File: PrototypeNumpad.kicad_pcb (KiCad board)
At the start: 2 copper layers, 99 x 99 mm, 86 parts, among them J0 Conn_01x06, J1 USB_B_Micro, SW0 SW_Push, U1 ATmega32U4-AU, U2 USBLC6-2SC6, Y1 Crystal_GND24

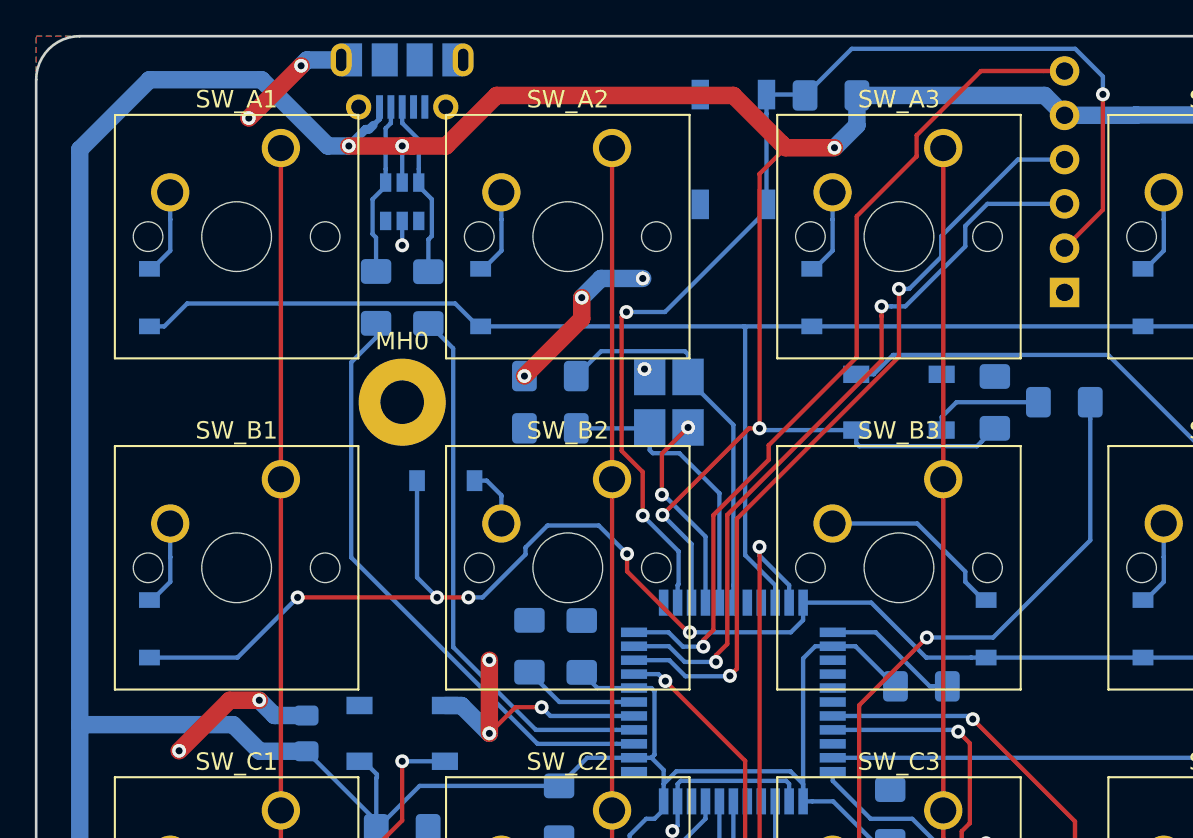
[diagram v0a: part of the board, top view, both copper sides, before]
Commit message: Add Header References
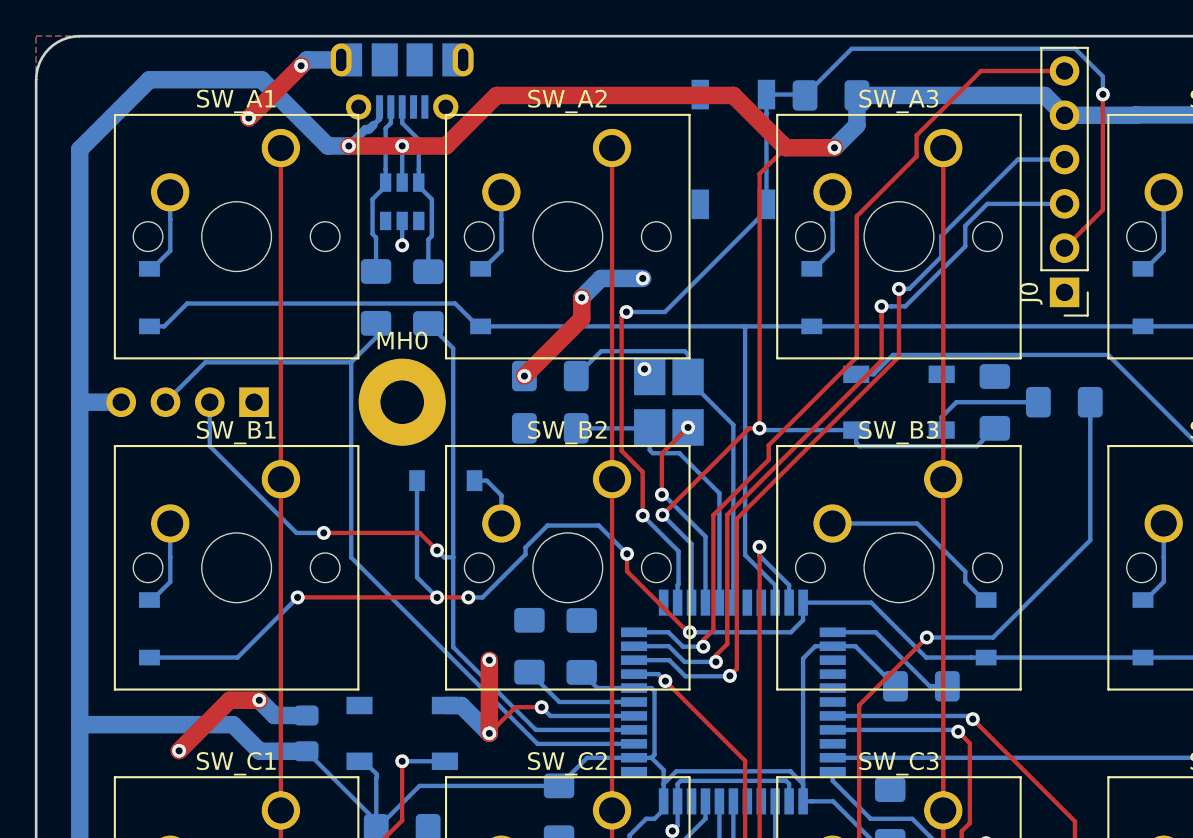
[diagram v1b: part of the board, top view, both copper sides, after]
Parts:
- added J1A1: Conn_01x04, Connector_PinHeader_2.54mm:PinHeader_1x04_P2.54mm_Vertical, B.Cu at (61.0, 49.5)
- J0: moved to F.Cu
- turned J0 to 180 degrees
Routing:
- net D+: track 31.5 -> 50.6 mm, vias 0 -> 2
- net D-: track 34.7 -> 46.3 mm
- net VCC: track 449.1 -> 451.5 mm
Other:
- board text added: "D+"
- board text added: "D-"
- board text added: "GND"
- board text added: "MISO"
- board text added: "MOSI"
- board text added: "RST"
- board text added: "SCK"
- board text added: "VCC"

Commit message: Re-position capacitor C9
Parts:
- moved C9 34.2 mm to (92.5, 49.5)
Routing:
- net GND: track 78.0 -> 69.2 mm, vias 20 -> 19
- net VCC: track 451.5 -> 449.5 mm
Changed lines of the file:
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@@
     (thickness 1.6)
     (drawings 18)
-    (tracks 657)
+    (tracks 649)
     (zones 0)
     (modules 87)
@@
   )
   (setup
-    (last_trace_width 0.25)
+    (last_trace_width 1)
     (user_trace_width 0.3)
     (user_trace_width 0.5)
@@
   )
   (module Capacitor_SMD:C_0805_2012Metric_Pad1.15x1.40mm_HandSolder (layer B.Cu)
-    (at 64 68.5 90)
+    (at 92.5 49.525 90)
     (descr "Capacitor SMD 0805 (2012 Metric), square (rectangular) end terminal, IPC_7351 nominal with elongated pad for handsoldering. (Body size source: https://docs.google.com/spreadsheets/d/1BsfQQcO9C6DZCsRaXUlFlo91Tg2WpOkGARC1WS5S8t0/edit?usp=sharing), generated with kicad-footprint-generator")
     (tags "capacitor handsolder")
@@
   (gr_line (start 51 28.5) (end 145 28.5) (layer Edge.Cuts) (width 0.15))
   (gr_line (start 51 127.5) (end 145 127.5) (layer Edge.Cuts) (width 0.15))
+  (via (at 78.5 74.5) (size 0.8) (drill 0.4) (layers F.Cu B.Cu) (net 1))
   (via (at 71 93) (size 0.8) (drill 0.4) (layers F.Cu B.Cu) (net 1))
   (via (at 83.4 47.6) (size 0.8) (drill 0.4) (layers F.Cu B.Cu) (net 1))
@@
   (via (at 60.7 33.2) (size 0.8) (drill 0.4) (layers F.Cu B.Cu) (net 1))
   (segment (start 60.7 33.2) (end 63.7 30.2) (width 1) (layer F.Cu) (net 1))
-  (via (at 61.3 66.6) (size 0.8) (drill 0.4) (layers F.Cu B.Cu) (net 1))
-  (segment (start 64 67.475) (end 62.175 67.475) (width 1) (layer B.Cu) (net 1))
-  (segment (start 62.175 67.475) (end 61.3 66.6) (width 1) (layer B.Cu) (net 1))
-  (via (at 56.7 69.5) (size 0.8) (drill 0.4) (layers F.Cu B.Cu) (net 1))
-  (segment (start 61.3 66.6) (end 59.6 66.6) (width 1) (layer F.Cu) (net 1))
-  (segment (start 59.6 66.6) (end 56.7 69.5) (width 1) (layer F.Cu) (net 1))
   (via (at 74.5 68.5) (size 0.8) (drill 0.4) (layers F.Cu B.Cu) (net 1))
   (segment (start 71.95 66.9) (end 72.9 66.9) (width 1) (layer B.Cu) (net 1))
@@
   (segment (start 69.5 34.8) (end 69.5 36.9) (width 0.25) (layer B.Cu) (net 4))
   (segment (start 68.0125 73.5375) (end 68.0125 74) (width 0.25) (layer B.Cu) (net 4))
-  (segment (start 64 69.525) (end 68.0125 73.5375) (width 0.25) (layer B.Cu) (net 4))
-  (segment (start 70.5 71.5125) (end 68.0125 74) (width 0.25) (layer B.Cu) (net 4))
-  (segment (start 78.5 71.5125) (end 70.5 71.5125) (width 0.25) (layer B.Cu) (net 4))
   (segment (start 80.1125 69.9) (end 82.8 69.9) (width 0.25) (layer B.Cu) (net 4))
   (segment (start 78.5 71.5125) (end 80.1125 69.9) (width 0.25) (layer B.Cu) (net 4))
-  (segment (start 67.3 70.1) (end 67.05 70.1) (width 0.25) (layer B.Cu) (net 4))
-  (segment (start 68.05 70.85) (end 67.3 70.1) (width 0.25) (layer B.Cu) (net 4))
-  (segment (start 68.05 71.025) (end 68.05 70.85) (width 0.25) (layer B.Cu) (net 4))
-  (segment (start 68.0125 71.0625) (end 68.05 71.025) (width 0.25) (layer B.Cu) (net 4))
-  (segment (start 68.0125 74) (end 68.0125 71.0625) (width 0.25) (layer B.Cu) (net 4))
   (segment (start 67.612001 33.837501) (end 67.843501 33.606001) (width 0.5) (layer B.Cu) (net 4))
   (segment (start 67.399999 33.837501) (end 67.612001 33.837501) (width 0.5) (layer B.Cu) (net 4))
@@
   (segment (start 65.232002 34.8) (end 66.4375 34.8) (width 1) (layer B.Cu) (net 4))
   (segment (start 61.432002 31) (end 65.232002 34.8) (width 1) (layer B.Cu) (net 4))
-  (segment (start 64 69.525) (end 61.322442 69.525) (width 1) (layer B.Cu) (net 4))
-  (segment (start 61.322442 69.525) (end 59.797442 68) (width 1) (layer B.Cu) (net 4))
-  (segment (start 59.797442 68) (end 51 68) (width 1) (layer B.Cu) (net 4))
   (segment (start 51 35) (end 55 31) (width 1) (layer B.Cu) (net 4))
   (segment (start 55 31) (end 61.432002 31) (width 1) (layer B.Cu) (net 4))
@@
   (segment (start 95.55 51.1) (end 95.55 51.85) (width 0.25) (layer B.Cu) (net 4))
   (via (at 90.000011 51) (size 0.8) (drill 0.4) (layers F.Cu B.Cu) (net 4))
-  (segment (start 95.55 51.1) (end 90.100011 51.1) (width 0.25) (layer B.Cu) (net 4))
   (segment (start 90.100011 51.1) (end 90.000011 51) (width 0.25) (layer B.Cu) (net 4))
   (via (at 84.433365 55.966638) (size 0.8) (drill 0.4) (layers F.Cu B.Cu) (net 4))
@@
   (segment (start 51 68) (end 51 49.5) (width 1) (layer B.Cu) (net 4))
   (segment (start 51 49.5) (end 51 35) (width 1) (layer B.Cu) (net 4))
+  (segment (start 92.5 50.55) (end 92.5 51.1) (width 0.25) (layer B.Cu) (net 4))
+  (segment (start 95.55 51.1) (end 92.5 51.1) (width 0.25) (layer B.Cu) (net 4))
+  (segment (start 92.5 51.1) (end 90.100011 51.1) (width 0.25) (layer B.Cu) (net 4))
+  (segment (start 53.1 70.1) (end 51 68) (width 1) (layer B.Cu) (net 4))
+  (segment (start 67.05 70.1) (end 53.1 70.1) (width 1) (layer B.Cu) (net 4))
+  (segment (start 67.05 73.0375) (end 68.0125 74) (width 1) (layer B.Cu) (net 4))
+  (segment (start 67.05 70.1) (end 67.05 73.0375) (width 1) (layer B.Cu) (net 4))
+  (segment (start 70.5 71.5125) (end 78.5 71.5125) (width 1) (layer B.Cu) (net 4))
+  (segment (start 68.0125 74) (end 70.5 71.5125) (width 1) (layer B.Cu) (net 4))
   (segment (start 78.5125 66.7) (end 82.8 66.7) (width 0.25) (layer B.Cu) (net 5))
   (segment (start 76.8 64.9875) (end 78.5125 66.7) (width 0.25) (layer B.Cu) (net 5))

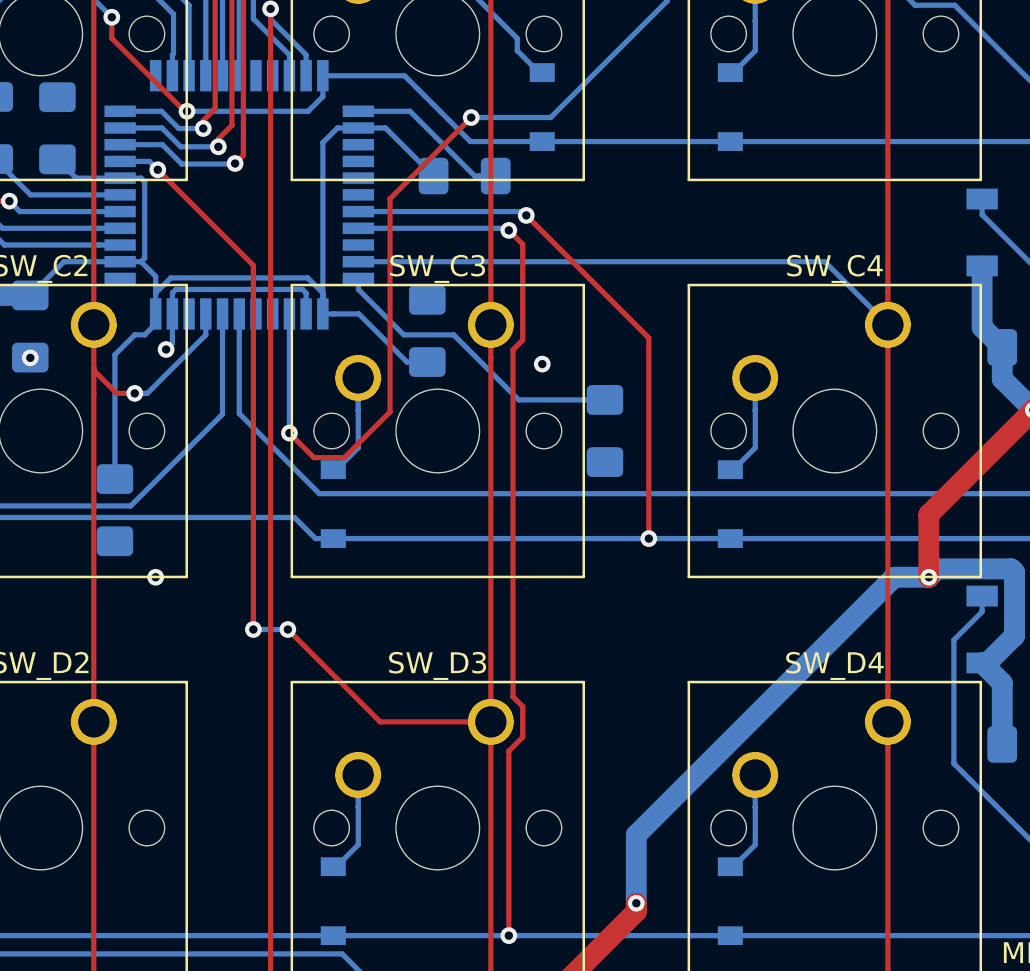
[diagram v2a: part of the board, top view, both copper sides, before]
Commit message: Add speaker to PCB
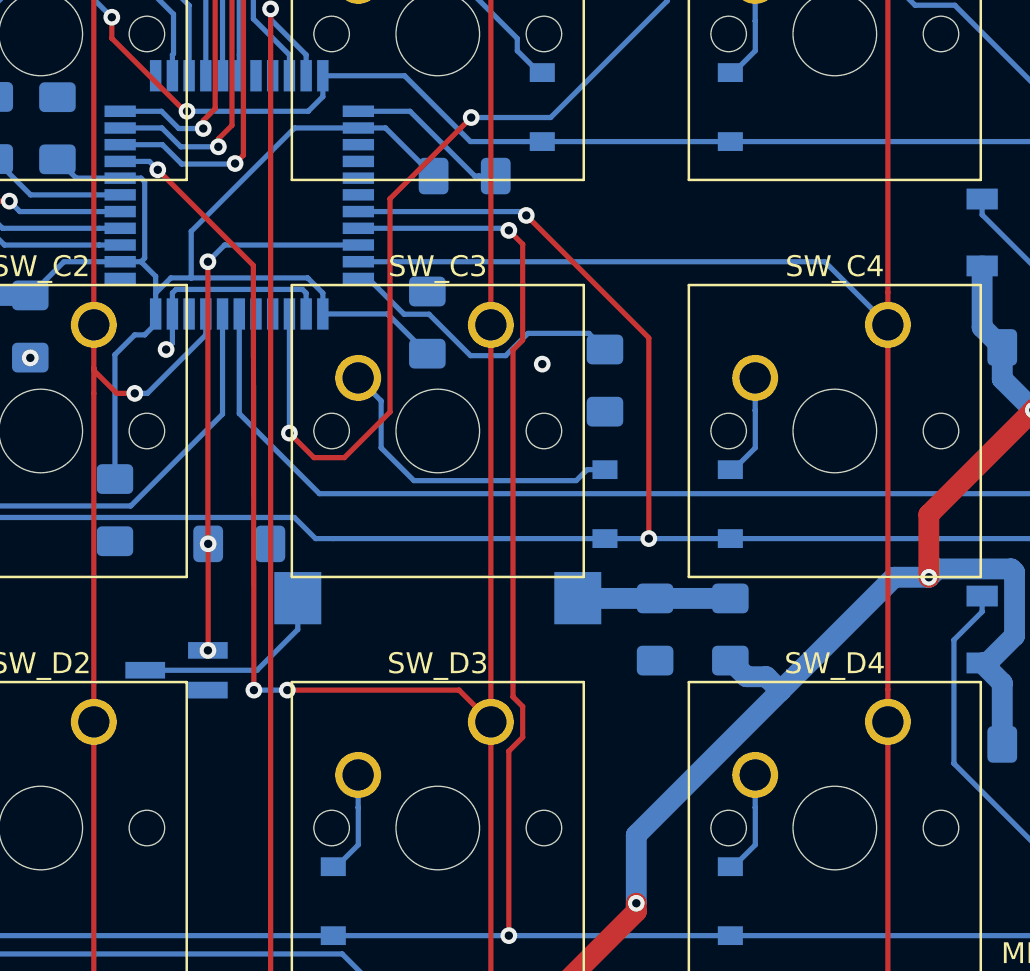
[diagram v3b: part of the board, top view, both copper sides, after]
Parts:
- added BZ1: Buzzer, Fate_Parts:Buzzer_AST1109MLTRQ, B.Cu at (98.0, 86.0)
- added C16: 10uF, Capacitor_SMD:C_1206_3216Metric_Pad1.42x1.75mm_HandSolder, B.Cu at (108.4, 87.5)
- added Q1: 2N7002, Package_TO_SOT_SMD:SOT-23_Handsoldering, B.Cu at (85.5, 89.5)
- added R6: 470, Resistor_SMD:R_1206_3216Metric_Pad1.42x1.75mm_HandSolder, B.Cu at (112.0, 87.5)
- added R7: 10K, Resistor_SMD:R_1206_3216Metric_Pad1.42x1.75mm_HandSolder, B.Cu at (88.5, 83.4)
- moved D_C3 13.0 mm to (106.0, 81.5)
- moved R4 2.41 mm to (106.0, 75.6)
- moved C6 0.40 mm to (97.5, 72.8)
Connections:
- U1 pad 31: Net-(U1-Pad31) -> SPEAKER
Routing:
- net SPEAKER: track 0.00 -> 26.2 mm, vias 0 -> 3
- net Net-(D_C3-Pad2): track 4.97 -> 15.4 mm
- net Net-(BZ1-Pad2): track 0.00 -> 9.61 mm
- net Net-(BZ1-Pad1): track 0.00 -> 7.31 mm
- net VCC: track 449.5 -> 454.4 mm
- net Col3: track 115.1 -> 116.7 mm
- net GND: vias 19 -> 18
